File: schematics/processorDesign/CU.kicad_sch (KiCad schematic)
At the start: 112 parts

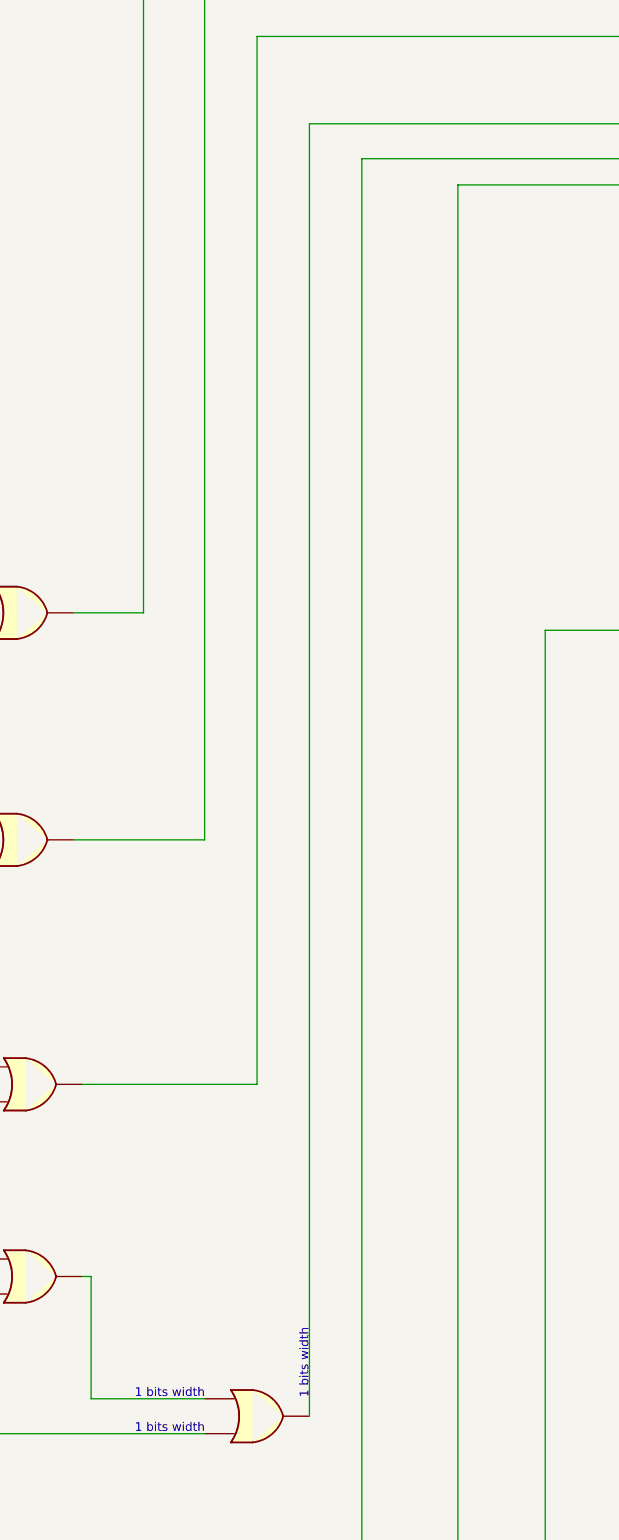
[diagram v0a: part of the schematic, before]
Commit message: added the IF stage and it's working properly
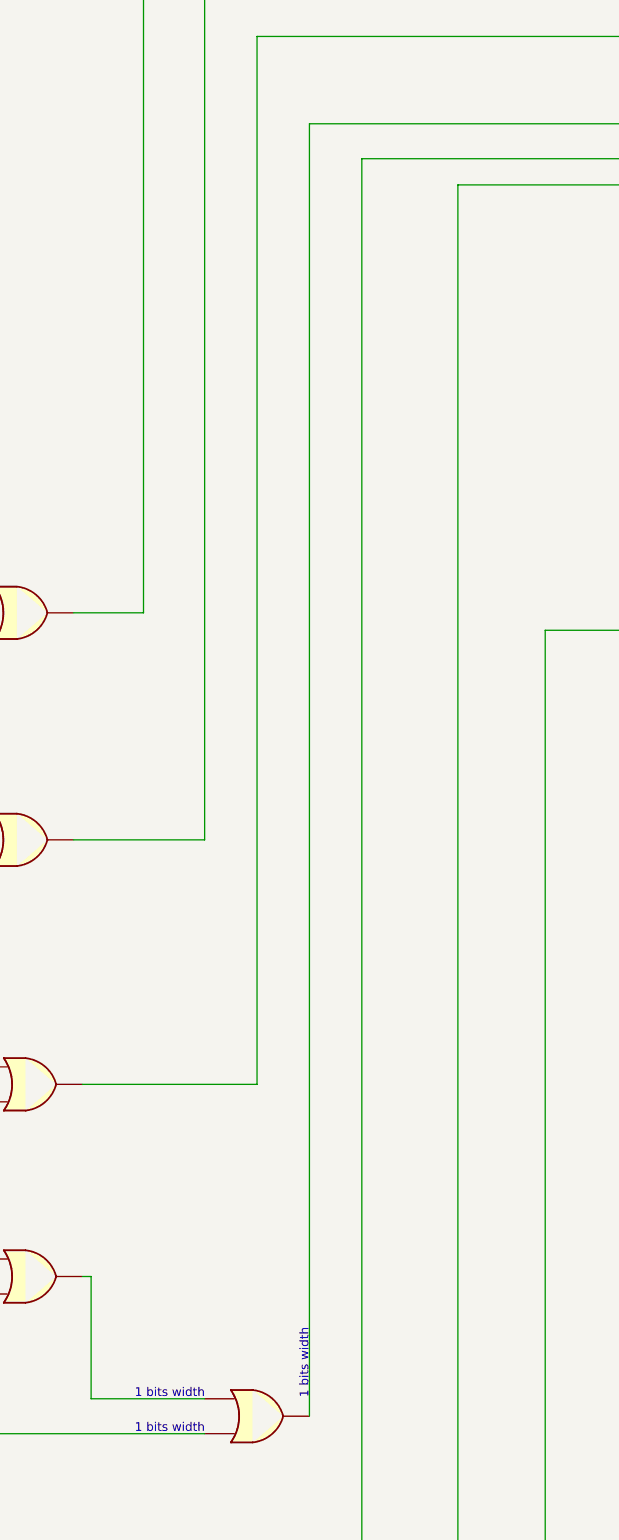
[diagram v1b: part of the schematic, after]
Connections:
- net at U?.: now also U?.2 (x4)
- net at U?.: now also U?.1 (x14)
- net at U?. (select): now also U?.2, U?.9
- net at U?.: now also U?.1, U?.1 (x2)
- net at U?. (select): now also U?.3, U?.8
- net at U?. (select): now also U?.3, U?.5
- new net: U?., U?. (select), U?.2
- new net: U?., U?. (select), U?.8
- now unconnected: U?., U?., U?. (select), U?. (select)
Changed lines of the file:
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@@
     (stroke (width 0) (type default) (color 0 0 0 0))
-  )
-  (wire (pts (xy 769.62 952.5) (xy 769.62 972.82))
-    (stroke (width 0) (type default) (color 180 176 85 1))
   )
   (wire (pts (xy 425.45 170.18) (xy 425.45 185.42))
@@
     (stroke (width 0) (type default) (color 0 0 0 0))
   )
-  (wire (pts (xy 769.62 952.5) (xy 769.62 784.86))
+  (wire (pts (xy 769.62 784.86) (xy 769.62 972.82))
     (stroke (width 0) (type default) (color 180 176 85 1))
   )

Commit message: the ID stage and ID_EX buffer are now working correctly until further testing
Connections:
- net at U?.: now also U?.2 (x4)
- net at U?.: now also U?.1 (x14)
- net at U?. (select): now also U?.2, U?.9
- net at U?.: now also U?.1, U?.1 (x2)
- net at U?. (select): now also U?.3, U?.8
- net at U?. (select): now also U?.3, U?.5
- new net: U?., U?. (select), U?.2
- new net: U?., U?. (select), U?.8
- now unconnected: U?., U?., U?. (select), U?. (select)

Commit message: the EX stage and EX_MEM is now complete till further testing
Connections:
- net at U?.: now also U?.2 (x4)
- net at U?.: now also U?.1 (x14)
- net at U?. (select): now also U?.2, U?.9
- net at U?.: now also U?.1, U?.1 (x2)
- net at U?. (select): now also U?.3, U?.8
- net at U?. (select): now also U?.3, U?.5
- new net: U?., U?. (select), U?.2
- new net: U?., U?. (select), U?.8
- now unconnected: U?., U?., U?. (select), U?. (select)

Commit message: the MEM stage and MEM_WB buffer are now correctly working for command LDM and still under testing
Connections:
- net at U?.: now also U?.2 (x4)
- net at U?.: now also U?.1 (x14)
- net at U?. (select): now also U?.2, U?.9
- net at U?.: now also U?.1, U?.1 (x2)
- net at U?. (select): now also U?.3, U?.8
- net at U?. (select): now also U?.3, U?.5
- new net: U?., U?. (select), U?.2
- new net: U?., U?. (select), U?.8
- now unconnected: U?., U?., U?. (select), U?. (select)

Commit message: the pipeline processor is semi-working for phase 1 to be complete, just there is a small bug in the command called std
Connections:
- net at U?.: now also U?.2 (x4)
- net at U?.: now also U?.1 (x14)
- net at U?. (select): now also U?.2, U?.9
- net at U?.: now also U?.1, U?.1 (x2)
- net at U?. (select): now also U?.3, U?.8
- net at U?. (select): now also U?.3, U?.5
- new net: U?., U?. (select), U?.2
- new net: U?., U?. (select), U?.8
- now unconnected: U?., U?., U?. (select), U?. (select)

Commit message: edited the priority of the flags for the CCR
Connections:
- net at U?.: now also U?.2 (x4)
- net at U?.: now also U?.1 (x14)
- net at U?. (select): now also U?.2, U?.9
- net at U?.: now also U?.1, U?.1 (x2)
- net at U?. (select): now also U?.3, U?.8
- net at U?. (select): now also U?.3, U?.5
- new net: U?., U?. (select), U?.2
- new net: U?., U?. (select), U?.8
- now unconnected: U?., U?., U?. (select), U?. (select)

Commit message: initially integrated processor without being tested
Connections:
- net at U?.: now also U?.2 (x4)
- net at U?.: now also U?.1 (x14)
- net at U?. (select): now also U?.2, U?.9
- net at U?.: now also U?.1, U?.1 (x2)
- net at U?. (select): now also U?.3, U?.8
- net at U?. (select): now also U?.3, U?.5
- new net: U?., U?. (select), U?.2
- new net: U?., U?. (select), U?.8
- now unconnected: U?., U?., U?. (select), U?. (select)

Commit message: test12
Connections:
- net SET_INT: no longer U?.9
- net at U?.: now also U?.2 (x4)
- net at U?.: now also U?.1 (x14)
- net at U?. (select): now also U?.2, U?.9
- net at U?.: now also U?.1, U?.1 (x2)
- net at U?. (select): now also U?.3, U?.8
- net at U?. (select): now also U?.3, U?.5
- net CLR_INT renamed CLR_OVF
- new net: U?., U?. (select), U?.2
- new net: U?., U?. (select), U?.8
- new net SET_OVF: U?.9
- now unconnected: U?., U?., U?. (select), U?. (select)
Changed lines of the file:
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@@
     (effects (font (size 1.27 1.27)) (justify left bottom))
+  )
+  (text "1 bit width" (at 1145.54 906.78 180)
+    (effects (font (size 1.27 1.27)) (justify right bottom))
   )
   (text "instr[8] 1 bits width (PC)" (at 689.61 979.17 180)
@@
     (effects (font (size 2 2)) (justify left))
   )
+  (hierarchical_label "SET_INT" (shape output) (at 1145.54 906.78 0)
+    (effects (font (size 2 2)) (justify left))
+  )
   (hierarchical_label "MemToReg" (shape output) (at 1149.35 306.07 0)
     (effects (font (size 2 2)) (justify left))
@@
     (effects (font (size 2 2)) (justify left))
   )
-  (hierarchical_label "SET_INT" (shape output) (at 1148.08 723.9 0)
+  (hierarchical_label "SET_OVF" (shape output) (at 1148.08 723.9 0)
     (effects (font (size 2 2)) (justify left))
   )
@@
     (effects (font (size 2 2)) (justify left))
   )
-  (hierarchical_label "CLR_INT" (shape output) (at 1148.08 784.86 0)
-    (effects (font (size 2 2)) (justify left))
-  )
+  (hierarchical_label "CLR_OVF" (shape output) (at 1148.08 784.86 0)
+    (effects (font (size 2 2)) (justify left))
+  )
